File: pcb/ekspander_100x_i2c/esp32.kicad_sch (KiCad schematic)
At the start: 7 parts, among them IC1 ESP32-S3-WROOM-1U-N16R8, U13 AP63203WU

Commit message: Ekspander 100x - zasilanie 3V3
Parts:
- added C7: 1uF_50V, Capacitor_THT:C_Disc_D5.0mm_W2.5mm_P5.00mm, symbol Device:C
- added C8: 22uF, 1_tme:RDEC71H226MWK1H03B, symbol Device:C
- added C9: 0.1uF, 1_tme:RDEC71H226MWK1H03B, symbol Device:C
- added R1: 10K, 1_tme:RESAD1520W50L600D230, symbol Device:R
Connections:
- net +3V3: now also C8.2, C9.2, R1.1
- net GND: now also C7.2, C8.1, C9.1
- net USB_D_N: now reaches IC1.13 (IO19)
- net USB_D_P: now reaches IC1.14 (IO20)
- net at IC1.3 (EN): now also C7.1, R1.2
- net SDA: now reaches IC1.4 (IO4)
- net SCK: now reaches IC1.5 (IO5)
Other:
- moved on the sheet: IC1

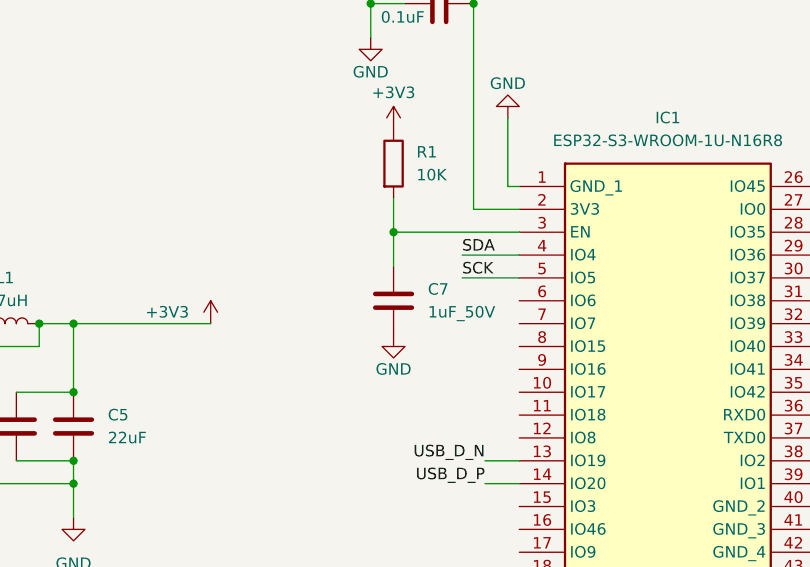
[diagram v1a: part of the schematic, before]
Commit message: Ekspander U2 - U3 - U4 update
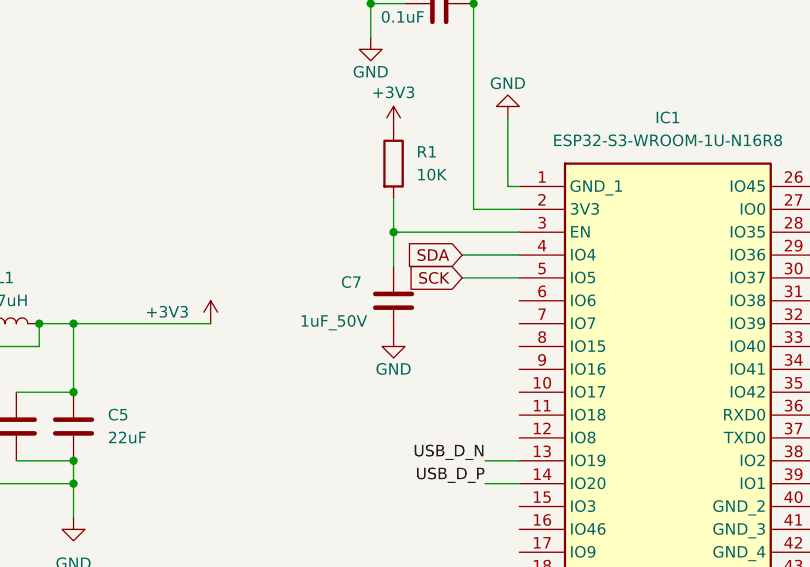
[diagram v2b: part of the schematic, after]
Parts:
- C3: footprint 1_tme:RDEC71H106K3P1H03B -> Capacitor_SMD:C_0805_2012Metric_Pad1.18x1.45mm_HandSolder
- C4: footprint Capacitor_THT:C_Disc_D3.8mm_W2.6mm_P2.50mm -> Capacitor_SMD:C_0805_2012Metric_Pad1.18x1.45mm_HandSolder
- C5, C6, C8, C9: footprint 1_tme:RDEC71H226MWK1H03B -> Capacitor_SMD:C_0805_2012Metric_Pad1.18x1.45mm_HandSolder
- C7: footprint Capacitor_THT:C_Disc_D5.0mm_W2.5mm_P5.00mm -> Capacitor_SMD:C_0805_2012Metric_Pad1.18x1.45mm_HandSolder
- R1: footprint 1_tme:RESAD1520W50L600D230 -> PCM_Resistor_SMD_AKL:R_0805_2012Metric_Pad1.20x1.40mm_HandSolder
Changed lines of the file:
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@@
 		)
 	)
-	(label "SCK"
-		(at 137.16 66.04 0)
+	(global_label "SDA"
+		(shape input)
+		(at 137.16 63.5 180)
+		(fields_autoplaced yes)
 		(effects
 			(font
 				(size 1.27 1.27)
 			)
-			(justify left bottom)
-		)
-	)
-	(label "SDA"
-		(at 137.16 63.5 0)
+			(justify right)
+		)
+		(property "Intersheetrefs" "${INTERSHEET_REFS}"
+			(at 130.6067 63.5 0)
+			(effects
+				(font
+					(size 1.27 1.27)
+				)
+				(justify right)
+				(hide yes)
+			)
+		)
+	)
+	(global_label "SCK"
+		(shape input)
+		(at 137.16 66.04 180)
+		(fields_autoplaced yes)
 		(effects
 			(font
 				(size 1.27 1.27)
 			)
-			(justify left bottom)
+			(justify right)
+		)
+		(property "Intersheetrefs" "${INTERSHEET_REFS}"
+			(at 130.4253 66.04 0)
+			(effects
+				(font
+					(size 1.27 1.27)
+				)
+				(justify right)
+				(hide yes)
+			)
 		)
 	)
@@
 			)
 		)
-		(property "Footprint" "1_tme:RDEC71H226MWK1H03B"
+		(property "Footprint" "Capacitor_SMD:C_0805_2012Metric_Pad1.18x1.45mm_HandSolder"
 			(at 138.43 34.5948 0)
 			(effects
@@
 		(on_board yes)
 		(dnp no)
-		(fields_autoplaced yes)
 		(property "Reference" "C7"
-			(at 133.35 67.3099 0)
+			(at 123.698 66.548 0)
 			(effects
 				(font
@@
 		)
 		(property "Value" "1uF_50V"
-			(at 133.35 69.8499 0)
+			(at 119.126 70.866 0)
 			(effects
 				(font
@@
 			)
 		)
-		(property "Footprint" "Capacitor_THT:C_Disc_D5.0mm_W2.5mm_P5.00mm"
+		(property "Footprint" "Capacitor_SMD:C_0805_2012Metric_Pad1.18x1.45mm_HandSolder"
 			(at 130.5052 72.39 0)
 			(effects
@@
 			)
 		)
-		(property "Footprint" "1_tme:RDEC71H106K3P1H03B"
+		(property "Footprint" "Capacitor_SMD:C_0805_2012Metric_Pad1.18x1.45mm_HandSolder"
 			(at 40.3352 80.01 0)
 			(effects
@@
 			)
 		)
-		(property "Footprint" "1_tme:RESAD1520W50L600D230"
+		(property "Footprint" "PCM_Resistor_SMD_AKL:R_0805_2012Metric_Pad1.20x1.40mm_HandSolder"
 			(at 127.762 53.34 90)
 			(effects
@@
 			)
 		)
-		(property "Footprint" "1_tme:RDEC71H226MWK1H03B"
+		(property "Footprint" "Capacitor_SMD:C_0805_2012Metric_Pad1.18x1.45mm_HandSolder"
 			(at 94.9452 86.36 0)
 			(effects
@@
 			)
 		)
-		(property "Footprint" "Capacitor_THT:C_Disc_D3.8mm_W2.6mm_P2.50mm"
+		(property "Footprint" "Capacitor_SMD:C_0805_2012Metric_Pad1.18x1.45mm_HandSolder"
 			(at 77.1652 67.31 0)
 			(effects
@@
 			)
 		)
-		(property "Footprint" "1_tme:RDEC71H226MWK1H03B"
+		(property "Footprint" "Capacitor_SMD:C_0805_2012Metric_Pad1.18x1.45mm_HandSolder"
 			(at 88.5952 86.36 0)
 			(effects
@@
 			)
 		)
-		(property "Footprint" "1_tme:RDEC71H226MWK1H03B"
+		(property "Footprint" "Capacitor_SMD:C_0805_2012Metric_Pad1.18x1.45mm_HandSolder"
 			(at 138.43 28.2448 0)
 			(effects

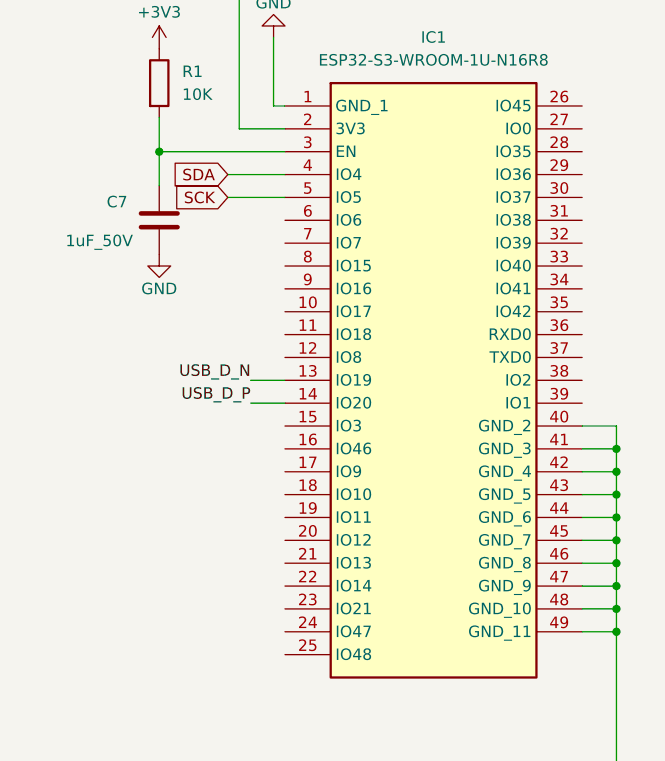
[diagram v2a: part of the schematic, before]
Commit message: Ekspander 24V update
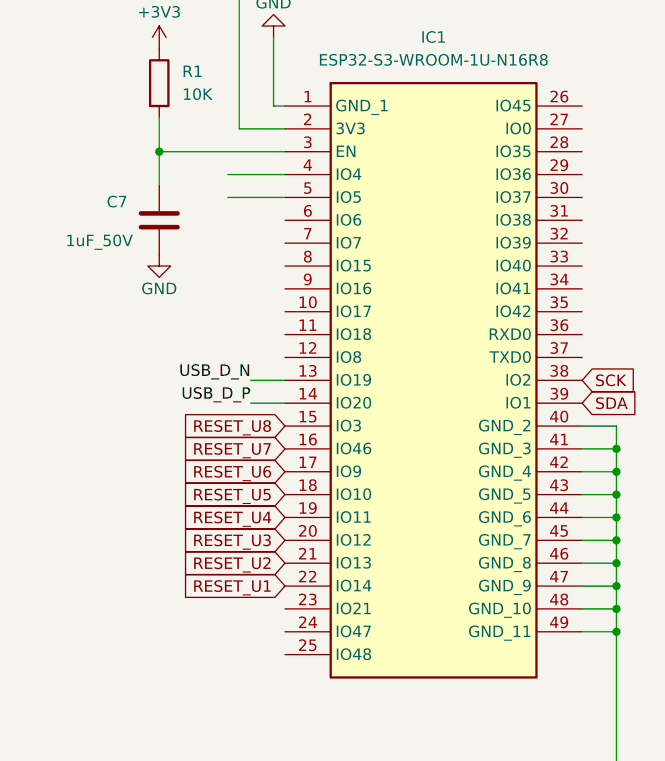
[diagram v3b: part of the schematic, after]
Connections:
- net SCK: now also IC1.38 (IO2); no longer IC1.5 (IO5)
- net SDA: now also IC1.39 (IO1); no longer IC1.4 (IO4)
- net RESET_U8: now reaches IC1.15 (IO3)
- net RESET_U7: now reaches IC1.16 (IO46)
- net RESET_U6: now reaches IC1.17 (IO9)
- net RESET_U5: now reaches IC1.18 (IO10)
- net RESET_U4: now reaches IC1.19 (IO11)
- net RESET_U3: now reaches IC1.20 (IO12)
- net RESET_U2: now reaches IC1.21 (IO13)
- net RESET_U1: now reaches IC1.22 (IO14)
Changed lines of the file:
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@@
+		)
+	)
+	(global_label "RESET_U6"
+		(shape input)
+		(at 143.51 96.52 180)
+		(fields_autoplaced yes)
+		(effects
+			(font
+				(size 1.27 1.27)
+			)
+			(justify right)
+		)
+		(property "Intersheetrefs" "${INTERSHEET_REFS}"
+			(at 131.2721 96.52 0)
+			(effects
+				(font
+					(size 1.27 1.27)
+				)
+				(justify right)
+				(hide yes)
+			)
+		)
+	)
+	(global_label "RESET_U8"
+		(shape input)
+		(at 143.51 91.44 180)
+		(fields_autoplaced yes)
+		(effects
+			(font
+				(size 1.27 1.27)
+			)
+			(justify right)
+		)
+		(property "Intersheetrefs" "${INTERSHEET_REFS}"
+			(at 131.2721 91.44 0)
+			(effects
+				(font
+					(size 1.27 1.27)
+				)
+				(justify right)
+				(hide yes)
+			)
+		)
+	)
+	(global_label "SCK"
+		(shape input)
+		(at 176.53 86.36 0)
+		(fields_autoplaced yes)
+		(effects
+			(font
+				(size 1.27 1.27)
+			)
+			(justify left)
+		)
+		(property "Intersheetrefs" "${INTERSHEET_REFS}"
+			(at 183.2647 86.36 0)
+			(effects
+				(font
+					(size 1.27 1.27)
+				)
+				(justify left)
+				(hide yes)
+			)
+		)
+	)
+	(global_label "RESET_U1"
+		(shape input)
+		(at 143.51 109.22 180)
+		(fields_autoplaced yes)
+		(effects
+			(font
+				(size 1.27 1.27)
+			)
+			(justify right)
+		)
+		(property "Intersheetrefs" "${INTERSHEET_REFS}"
+			(at 131.2721 109.22 0)
+			(effects
+				(font
+					(size 1.27 1.27)
+				)
+				(justify right)
+				(hide yes)
+			)
+		)
+	)
+	(global_label "RESET_U2"
+		(shape input)
+		(at 143.51 106.68 180)
+		(fields_autoplaced yes)
+		(effects
+			(font
+				(size 1.27 1.27)
+			)
+			(justify right)
+		)
+		(property "Intersheetrefs" "${INTERSHEET_REFS}"
+			(at 131.2721 106.68 0)
+			(effects
+				(font
+					(size 1.27 1.27)
+				)
+				(justify right)
+				(hide yes)
+			)
+		)
+	)
+	(global_label "RESET_U3"
+		(shape input)
+		(at 143.51 104.14 180)
+		(fields_autoplaced yes)
+		(effects
+			(font
+				(size 1.27 1.27)
+			)
+			(justify right)
+		)
+		(property "Intersheetrefs" "${INTERSHEET_REFS}"
+			(at 131.2721 104.14 0)
+			(effects
+				(font
+					(size 1.27 1.27)
+				)
+				(justify right)
+				(hide yes)
+			)
+		)
+	)
+	(global_label "RESET_U7"
+		(shape input)
+		(at 143.51 93.98 180)
+		(fields_autoplaced yes)
+		(effects
+			(font
+				(size 1.27 1.27)
+			)
+			(justify right)
+		)
+		(property "Intersheetrefs" "${INTERSHEET_REFS}"
+			(at 131.2721 93.98 0)
+			(effects
+				(font
+					(size 1.27 1.27)
+				)
+				(justify right)
+				(hide yes)
+			)
+		)
+	)
+	(global_label "RESET_U5"
+		(shape input)
+		(at 143.51 99.06 180)
+		(fields_autoplaced yes)
+		(effects
+			(font
+				(size 1.27 1.27)
+			)
+			(justify right)
+		)
+		(property "Intersheetrefs" "${INTERSHEET_REFS}"
+			(at 131.2721 99.06 0)
+			(effects
+				(font
+					(size 1.27 1.27)
+				)
+				(justify right)
+				(hide yes)
+			)
+		)
+	)
+	(global_label "RESET_U4"
+		(shape input)
+		(at 143.51 101.6 180)
+		(fields_autoplaced yes)
+		(effects
+			(font
+				(size 1.27 1.27)
+			)
+			(justify right)
+		)
+		(property "Intersheetrefs" "${INTERSHEET_REFS}"
+			(at 131.2721 101.6 0)
+			(effects
+				(font
+					(size 1.27 1.27)
+				)
+				(justify right)
+				(hide yes)
+			)
 		)
 	)
 	(global_label "SDA"
 		(shape input)
-		(at 137.16 63.5 180)
-		(fields_autoplaced yes)
-		(effects
-			(font
-				(size 1.27 1.27)
-			)
-			(justify right)
-		)
-		(property "Intersheetrefs" "${INTERSHEET_REFS}"
-			(at 130.6067 63.5 0)
-			(effects
-				(font
-					(size 1.27 1.27)
-				)
-				(justify right)
-				(hide yes)
-			)
-		)
-	)
-	(global_label "SCK"
-		(shape input)
-		(at 137.16 66.04 180)
-		(fields_autoplaced yes)
-		(effects
-			(font
-				(size 1.27 1.27)
-			)
-			(justify right)
-		)
-		(property "Intersheetrefs" "${INTERSHEET_REFS}"
-			(at 130.4253 66.04 0)
-			(effects
-				(font
-					(size 1.27 1.27)
-				)
-				(justify right)
-				(hide yes)
-			)
+		(at 176.53 88.9 0)
+		(fields_autoplaced yes)
+		(effects
+			(font
+				(size 1.27 1.27)
+			)
+			(justify left)
+		)
+		(property "Intersheetrefs" "${INTERSHEET_REFS}"
+			(at 183.0833 88.9 0)
+			(effects
+				(font
+					(size 1.27 1.27)
+				)
+				(justify left)
+				(hide yes)
+			)

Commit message: Remove temporary and backup files, update component properties in the I2C ekspander PCB design, and enhance the CSV with additional component details.
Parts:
- IC1: Cena (none) -> 24
- L1: Link (none) -> https://www.tme.eu/pl/details/lsxnd6060yel4r7nmg/dlawiki/ta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
- R1: Cena (none) -> 0,04
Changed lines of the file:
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@@
 			)
 		)
-		(property "Datasheet" "~"
+		(property "Datasheet" "https://www.tme.eu/Document/3e9c82fa3e4673c31af8686f4595edf5/LSXN.pdf"
 			(at 86.36 71.12 0)
 			(effects
@@
 		(property "Description" "Inductor"
 			(at 86.36 71.12 0)
+			(effects
+				(font
+					(size 1.27 1.27)
+				)
+				(hide yes)
+			)
+		)
+		(property "Link" "https://www.tme.eu/pl/details/lsxnd6060yel4r7nmg/dlawiki/taiyo-yuden/"
+			(at 86.36 71.12 90)
 			(effects
 				(font
@@
 			)
 		)
+		(property "Cena" "0,04"
+			(at 129.54 53.34 0)
+			(effects
+				(font
+					(size 1.27 1.27)
+				)
+				(hide yes)
+			)
+		)
 		(pin "2"
 		)
@@
 				(hide yes)
 			)
+		)
+		(property "Cena" "24"
+			(at 143.51 55.88 0)
+			(effects
+				(font
+					(size 1.27 1.27)
+				)
+				(hide yes)
+			)

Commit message: Ekspander 100x - UART-USB
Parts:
- added C30: 1u, Capacitor_SMD:C_0805_2012Metric, symbol SparkFun-Capacitor:C
- added C32: 0.1u, Capacitor_SMD:C_0805_2012Metric, symbol SparkFun-Capacitor:C
- added C33: 4.7u, Footprints:T491A, symbol T491A106K010AT7280:T491A106K010AT7280
- added D5: Green, 1_tme:LEDC2012X120N, symbol LTST-C170GKT:LTST-C170GKT
- added D6: Red, 1_tme:LEDC2012X120N, symbol LTST-C170KRKT:LTST-C170KRKT
- added J25: USB4145-03-0230-C, USB4145030230C, symbol 1_tme:USB4145-03-0230-C
- added R10, R15: 5k1, Resistor_SMD:R_0805_2012Metric, symbol Device:R
- added R11: 1K, Resistor_SMD:R_0805_2012Metric, symbol Device:R
- added R12: 22K1, Resistor_SMD:R_0805_2012Metric, symbol Device:R
- added R13: 47K5, Resistor_SMD:R_0805_2012Metric, symbol Device:R
- added R14, R18: 330, Resistor_SMD:R_0805_2012Metric, symbol Device:R
- added U39: USBLC6-2SC6, Package_TO_SOT_SMD:SOT-23-6, symbol Power_Protection:USBLC6-2SC6
- added U41: CP2102N-A02-GQFN20, Package_DFN_QFN:SiliconLabs_QFN-20-1EP_3x3mm_P0.5mm_EP1.8x1.8mm, symbol Interface_USB:CP2102N-Axx-xQFN20
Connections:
- net +3V3: now also C32.1, C33.1 (+), D5.2 (A), D6.2 (A), R11.1, U41.6 (VDD), U41.7 (VREGIN)
- net GND: now also C30.2, C32.2, C33.2 (-), J25.A1 (GND_1), J25.A12 (GND_2), J25.B1 (GND_3), J25.B12 (GND_4), J25.MH1 (MH5), J25.MH2 (MH6), J25.MH3, J25.MH4, R10.2, R13.2, R15.2, U39.2 (GND), U41.12 (GND), U41.21 (GND), U41.3 (GND)
- net TX_RX: now reaches IC1.36 (RXD0)
- net TX_RX: now also U41.18 (TXD)
- net RX_TX: now reaches IC1.37 (TXD0)
- net RX_TX: now also U41.17 (RXD)
- net RTS: now reaches IC1.8 (IO15)
- net RTS: now also U41.16 (~{RTS})
- net DTS: now reaches IC1.9 (IO16)
- net DTS: now also U41.15 (~{CTS})
- new net: J25.A5 (CC1), R15.1
- new net: C30.1, R12.2, R13.1, U41.8 (VBUS)
- new net: R18.1, U41.19 (~{RXT}/GPIO.3)
- new net: R14.1, U41.20 (~{TXT}/GPIO.2)
- new net: R11.2, U41.9 (~{RST})
- new net: J25.B5 (CC2), R10.1
- new net: D6.1 (K), R18.2
- new net: D5.1 (K), R14.2
- new net USB_D+: U39.3 (I/O2), U41.4 (D+)
- new net USB_D-: U39.1 (I/O1), U41.5 (D-)
- new net USB_DN: J25.A7 (DN1), J25.B7 (DN2), U39.6 (I/O1)
- new net USB_DP: J25.A6 (DP1), J25.B6 (DP2), U39.4 (I/O2)
- new net VBUS: J25.A4 (VBUS_1), J25.A9 (VBUS_2), J25.B4 (VBUS_3), J25.B9 (VBUS_4), R12.1, U39.5 (VBUS)
- no-connect marks 0 -> 7
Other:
- note added: "Activity LEDs"
- moved on the sheet: C3, C4, C5, C6, C7, C8, C9, IC1, L1, R1, U13
